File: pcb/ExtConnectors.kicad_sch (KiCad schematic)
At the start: 12 parts, among them J1 USB_C_Receptacle_USB2.0_16P, U2 TPD2E2U06, U3 AP2112K-3.3, U6 TVS0500DRV, U7 TPD6E05U06RVZ

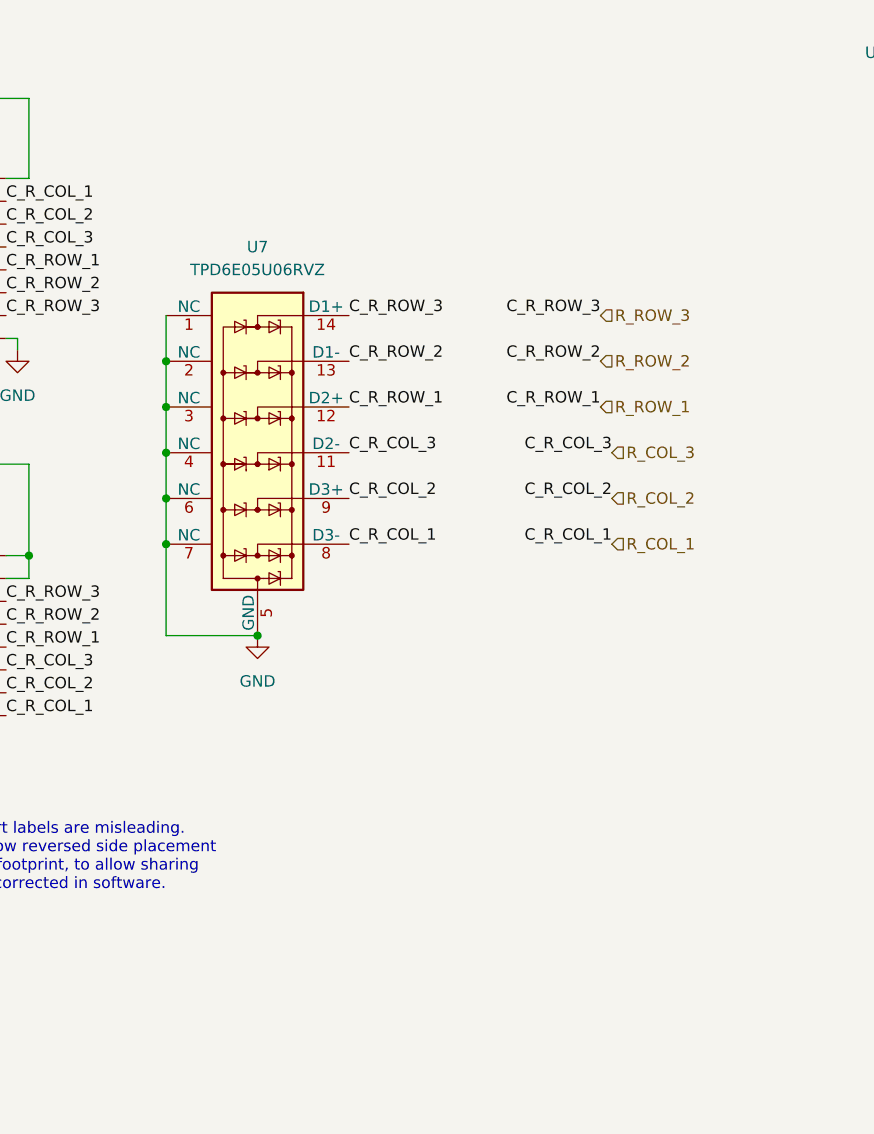
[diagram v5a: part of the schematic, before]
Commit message: Replacing 6 channel ESD protection with multiple 2 channel ones.
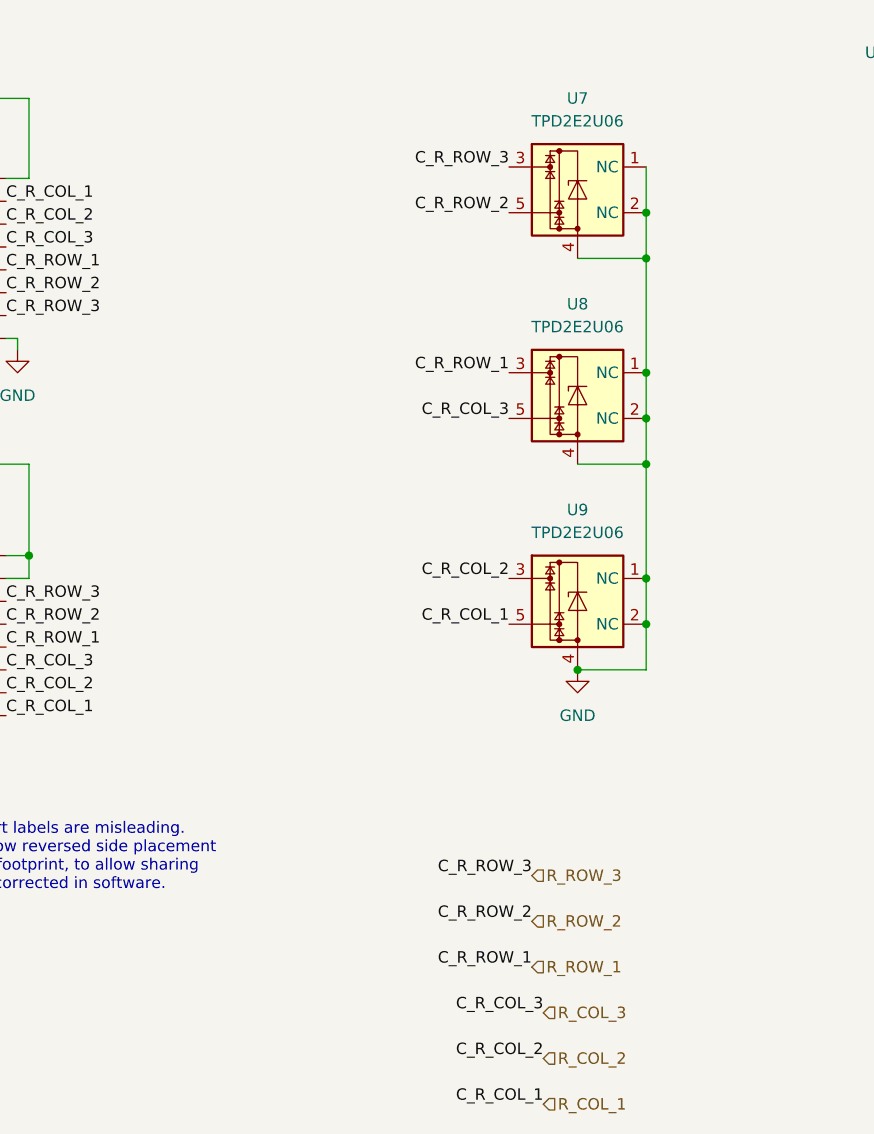
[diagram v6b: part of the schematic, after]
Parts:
- removed U7: TPD6E05U06RVZ, Package_SON:Texas_R-PUSON-N14, symbol Power_Protection:TPD6E05U06RVZ
- added U7, U8, U9: TPD2E2U06, Package_TO_SOT_SMD:SOT-553, symbol Power_Protection:TPD2E2U06
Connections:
- net GND: now also U7.1 (NC), U7.2 (NC), U7.4, U8.1 (NC), U8.2 (NC), U8.4, U9.1 (NC), U9.2 (NC), U9.4
- net R_COL_1: now also U9.5
- net R_COL_2: now also U9.3
- net R_COL_3: now also U8.5
- net R_ROW_1: now also U8.3
- net R_ROW_2: now also U7.5
- net R_ROW_3: now also U7.3

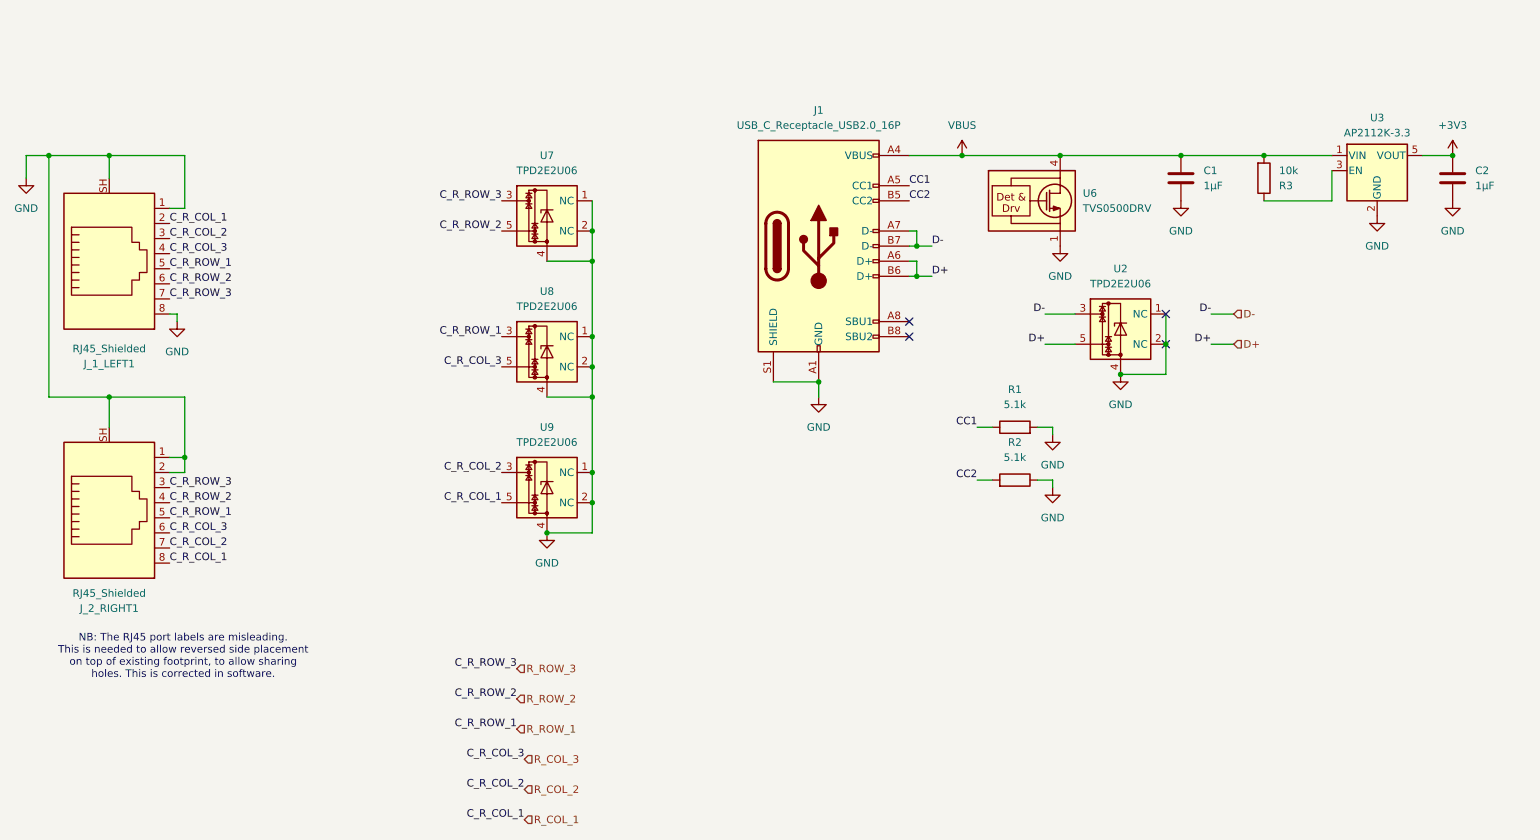
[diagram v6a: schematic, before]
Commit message: WIP: Starting to migrate toward 2 independant halves.
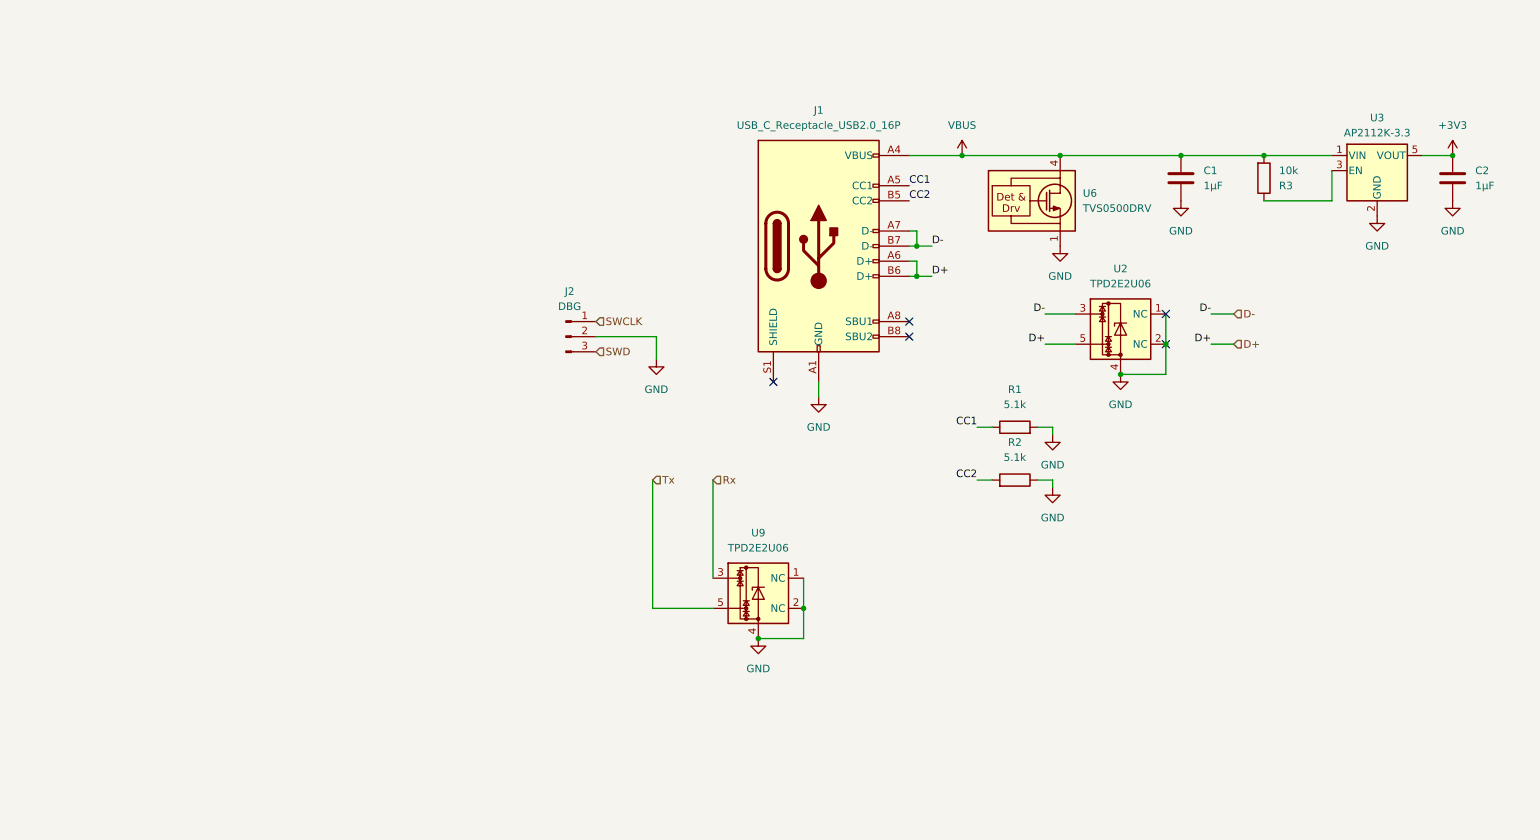
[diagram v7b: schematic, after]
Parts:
- removed J_1_LEFT1, J_2_RIGHT1: RJ45_Shielded, Connector_RJ:RJ45_Ninigi_GE, symbol Connector:RJ45_Shielded
- removed U7, U8: TPD2E2U06, Package_TO_SOT_SMD:SOT-553, symbol Power_Protection:TPD2E2U06
- added J2: DBG, Connector_PinHeader_2.54mm:PinHeader_1x03_P2.54mm_Vertical, symbol Connector:Conn_01x03_Pin
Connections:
- net GND: now also J2.2 (Pin_2); no longer J1.S1 (SHIELD)
- net R_COL_1 renamed Tx
- net R_COL_2 renamed Rx
- new net SWCLK: J2.1 (Pin_1)
- new net SWD: J2.3 (Pin_3)
- no-connect marks 4 -> 5
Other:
- note removed: "NB: The RJ45 port labels are misleading. This is needed to allow reversed side placement on top of existing footprint, to allow sharing holes. This is corrected in software."
- moved on the sheet: U9

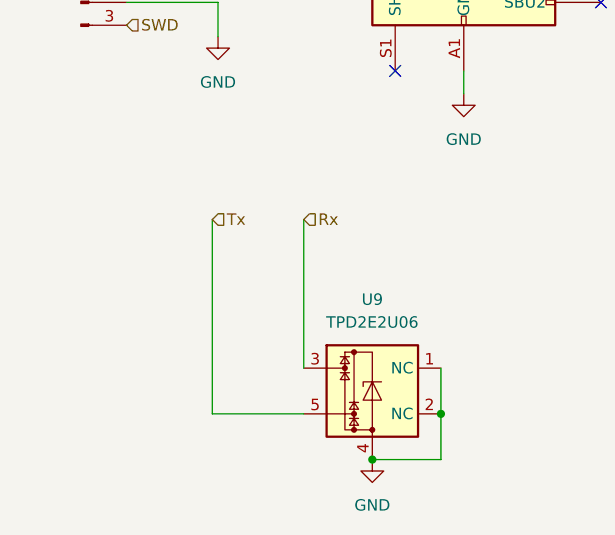
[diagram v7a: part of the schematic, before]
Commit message: WIP: Updating keyboard matrix to use the new shared part and reorganizing all the LED outputs.
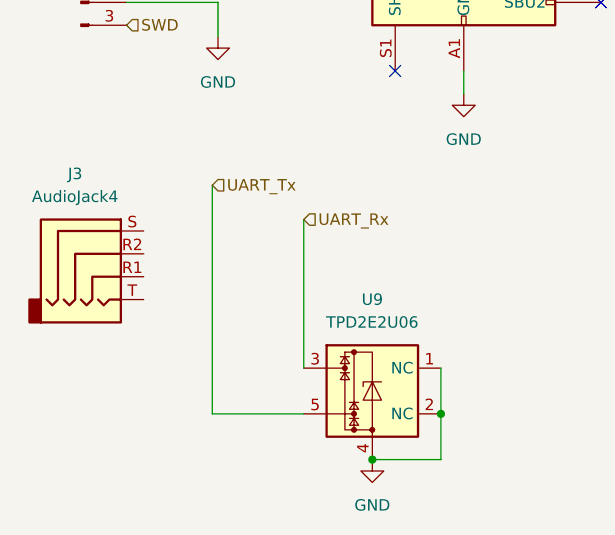
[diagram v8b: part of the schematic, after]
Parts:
- added J3: AudioJack4, symbol Connector_Audio:AudioJack4
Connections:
- net Rx renamed UART_Rx
- net Tx renamed UART_Tx
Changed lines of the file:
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@@
 	(wire
 		(pts
-			(xy 129.54 102.87) (xy 129.54 124.46)
+			(xy 129.54 99.06) (xy 129.54 124.46)
 		)
 		(stroke
@@
 		)
 	)
-	(hierarchical_label "Tx"
-		(shape input)
-		(at 129.54 102.87 0)
+	(hierarchical_label "UART_Tx"
+		(shape input)
+		(at 129.54 99.06 0)
 		(fields_autoplaced yes)
 		(effects
@@
 		)
 	)
-	(hierarchical_label "Rx"
+	(hierarchical_label "UART_Rx"
 		(shape input)
 		(at 139.7 102.87 0)
@@
 					(unit 1)
 				)
+			)
+		)
+	)
+	(symbol
+		(lib_id "Connector_Audio:AudioJack4")
+		(at 116.84 106.68 0)
+		(unit 1)
+		(exclude_from_sim no)
+		(in_bom yes)
+		(on_board yes)
+		(dnp no)
+		(fields_autoplaced yes)
+		(property "Reference" "J3"
+			(at 114.3 97.79 0)
+			(effects
+				(font
+					(size 1.27 1.27)
+				)
+			)
+		)
+		(property "Value" "AudioJack4"
+			(at 114.3 100.33 0)
+			(effects
+				(font
+					(size 1.27 1.27)
+				)
+			)
+		)
+		(property "Footprint" ""
+			(at 116.84 106.68 0)
+			(effects
+				(font
+					(size 1.27 1.27)
+				)
+				(hide yes)
+			)
+		)
+		(property "Datasheet" "~"
+			(at 116.84 106.68 0)
+			(effects
+				(font
+					(size 1.27 1.27)
+				)
+				(hide yes)
+			)
+		)
+		(property "Description" "Audio Jack, 4 Poles (TRRS)"
+			(at 116.84 106.68 0)
+			(effects
+				(font
+					(size 1.27 1.27)
+				)
+				(hide yes)
+			)
+		)
+		(pin "R2"
+		)
+		(pin "S"
+		)
+		(pin "R1"
+		)
+		(pin "T"
+		)
+		(instances
+			(project ""
+				(path "/9203b006-47ac-4f34-8cc4-2b709e3df56f/e6ab333d-5f1a-4b76-81c6-498aebdc0c3b"
+					(reference "J3")
+					(unit 1)
+				)
